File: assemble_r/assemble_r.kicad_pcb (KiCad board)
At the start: 2 copper layers, 128.5 x 102.6 mm, 50 parts, among them J23 Conn_01x02_Pin, SW23 SW_Push, SW24 SW_Push, SW25 SW_Push, SW26 SW_Push, SW27 SW_Push, SW28 SW_Push, SW29 SW_Push, SW30 SW_Push, SW31 SW_Push, SW32 SW_Push, SW33 SW_Push, SW34 SW_Push, SW35 SW_Push, SW36 SW_Push, SW37 SW_Push, SW38 SW_Push, SW39 SW_Push, SW40 SW_Push, SW41 SW_Push, SW42 SW_Push, SW43 SW_Push, SW44 SW_Push, U23 Micon_BLEMicroPro

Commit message: feat: update PCB
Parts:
- removed J23: Conn_01x02_Pin, kbd_Parts:Battery_2pin
- removed REF**: BatteryHolder_単4, kbd_Parts:Battery_AAA
- added AE-XCL: ~, kicad-lib:AE-XCL102D333CR-G, F.Cu at (58.5, 112.0)
- added BT1: Battery_Cell, kbd_Parts:Battery_AAA, F.Cu at (86.8, 55.4)
- added SW45: SW_SPDT, kbd_Parts:TGSW_MSK-12D19, F.Cu at (48.0, 114.5)
- moved SW44 4.85 mm to (48.5, 103.0)
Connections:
- U23 pad 26: GND -> Bat-

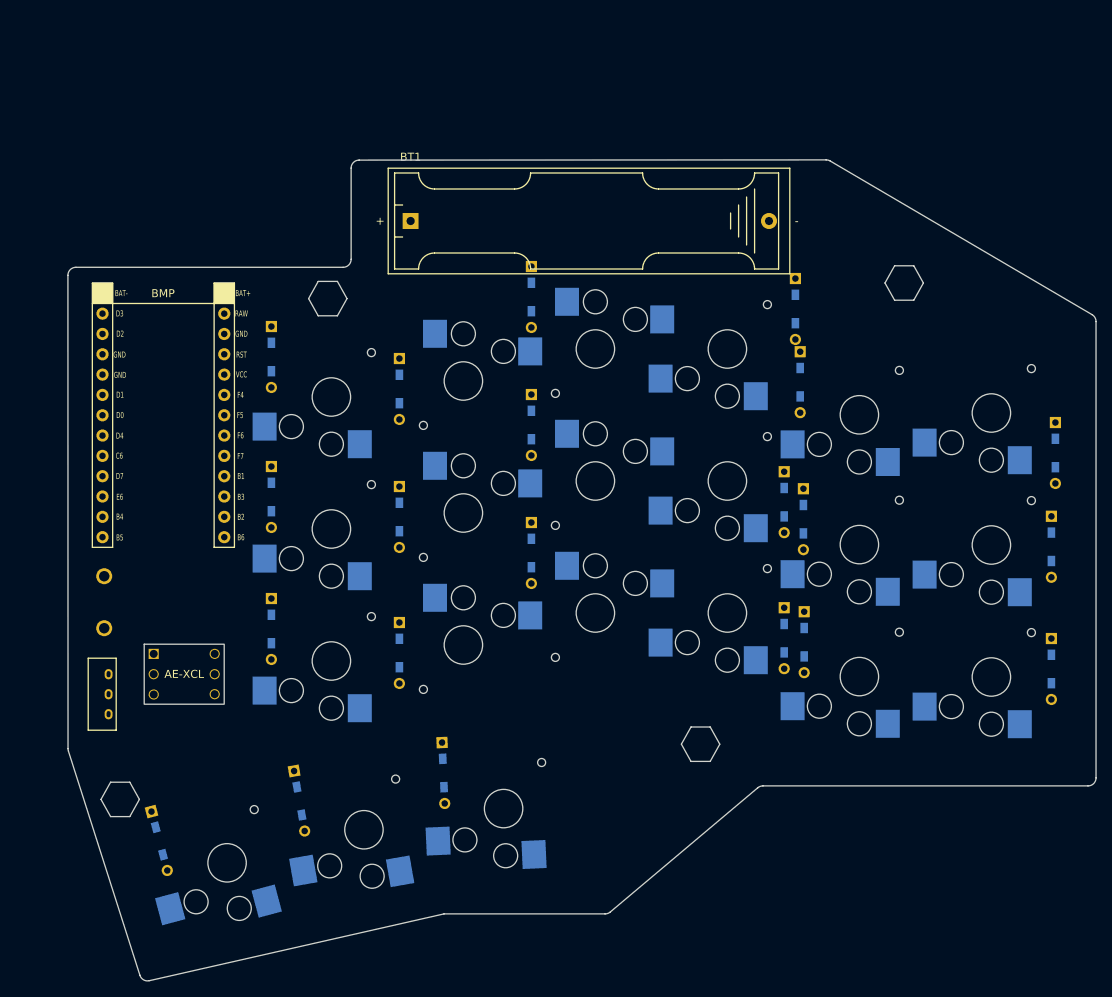
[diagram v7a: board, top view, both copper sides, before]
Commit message: fix: footprint of diode
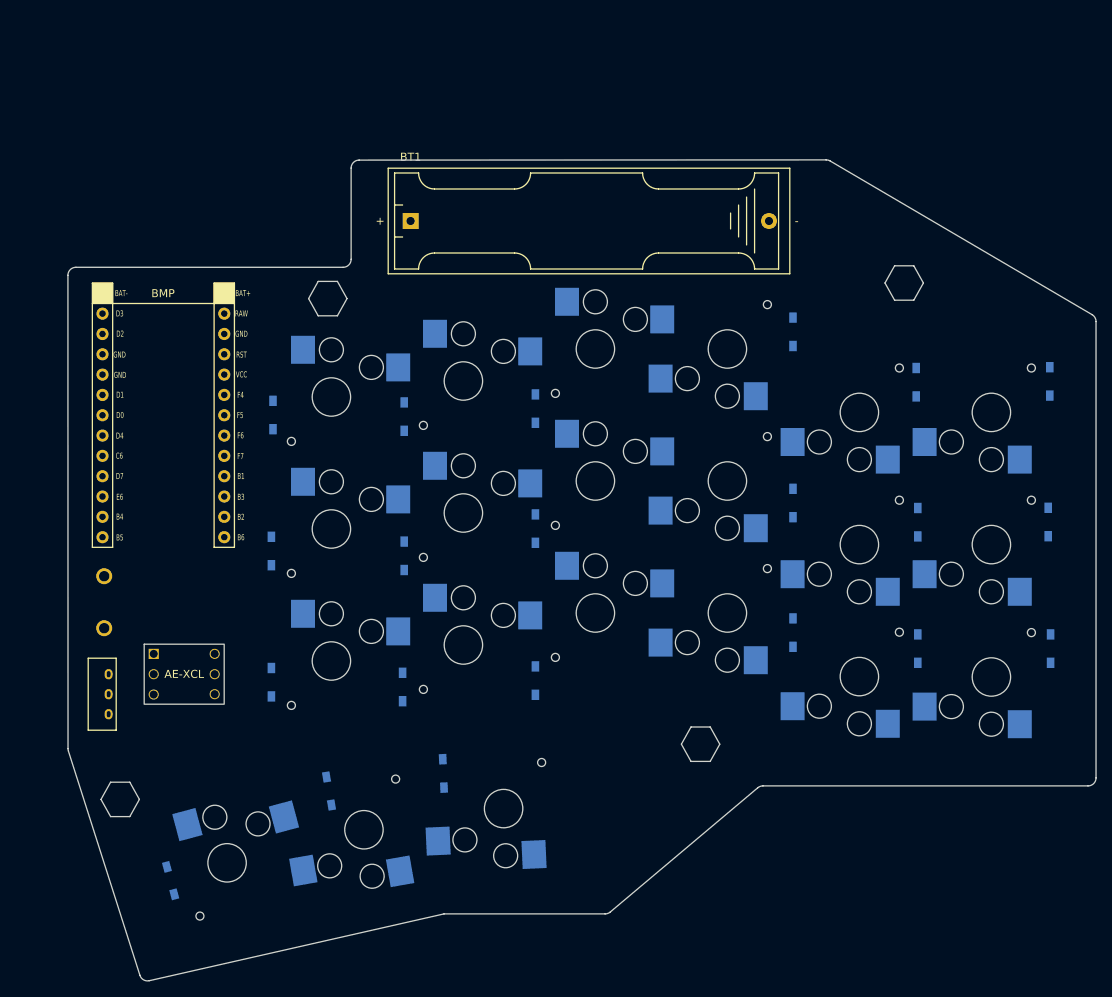
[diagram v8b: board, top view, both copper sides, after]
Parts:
- D23, D24, D25, D26, D27, D28, D29, D30, D31, D32, D33, D34, D35, D36, D37, D38, D39, D40, D41, D42, D43: footprint kbd_Parts:Diode_TH_SMD -> kbd_Parts:Diode_SMD
- moved D33 16.0 mm to (102.4, 112.8)
- moved D38 14.5 mm to (150.0, 75.5)
- moved D39 14.3 mm to (150.2, 93.0)
- moved D40 14.2 mm to (150.2, 108.8)
- moved D31 14.0 mm to (102.4, 78.8)
- moved D32 13.0 mm to (102.4, 93.8)
- moved D41 8.98 mm to (166.7, 75.4)
- moved D23 7.25 mm to (69.6, 79.6)
- moved D24 6.75 mm to (69.4, 96.6)
- moved D25 6.65 mm to (69.4, 113.0)
- moved D26 5.14 mm to (56.8, 137.8)
- moved D28 4.89 mm to (86.0, 97.2)
- moved D29 4.27 mm to (85.8, 113.6)
- moved D30 3.91 mm to (76.6, 126.6)
- moved D27 3.50 mm to (86.0, 79.8)
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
